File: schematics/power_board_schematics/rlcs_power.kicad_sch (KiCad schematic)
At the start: 39 parts, among them J1 Conn_01x05_Male, J2 Conn_01x05_Male, J4 Battery Conn, J5 Battery Conn, J6 CONN_01X02, J7 CONN_01X02, J8 CONN_01X02, Q1 Q_NPN_BEC, Q2 Q_NPN_BEC, T1 12 to 3v3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

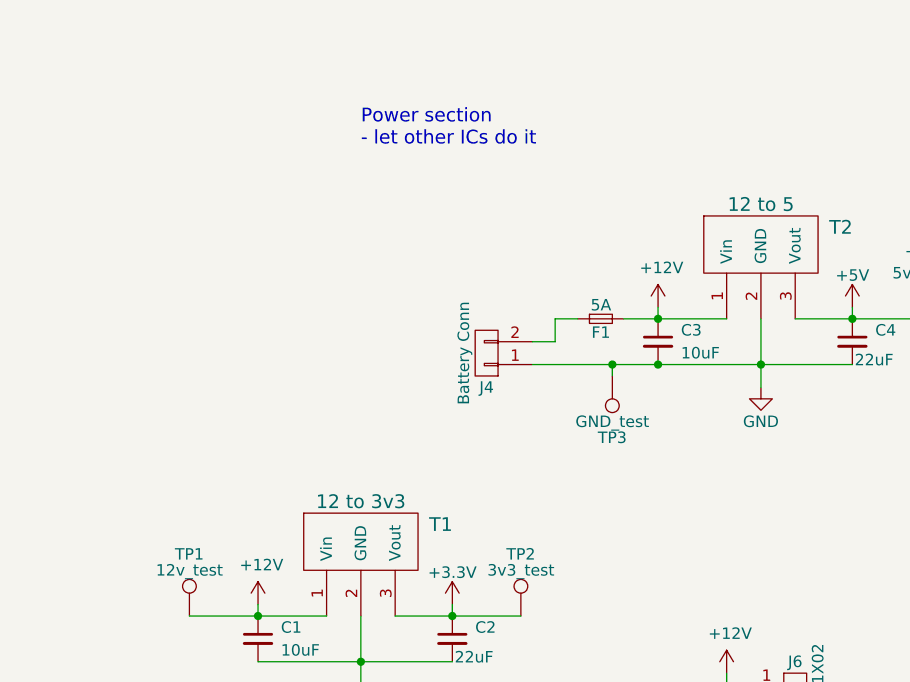
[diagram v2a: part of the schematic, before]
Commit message: Add Client Connection and Arm status indicator LED to Towerside Power Board schematic
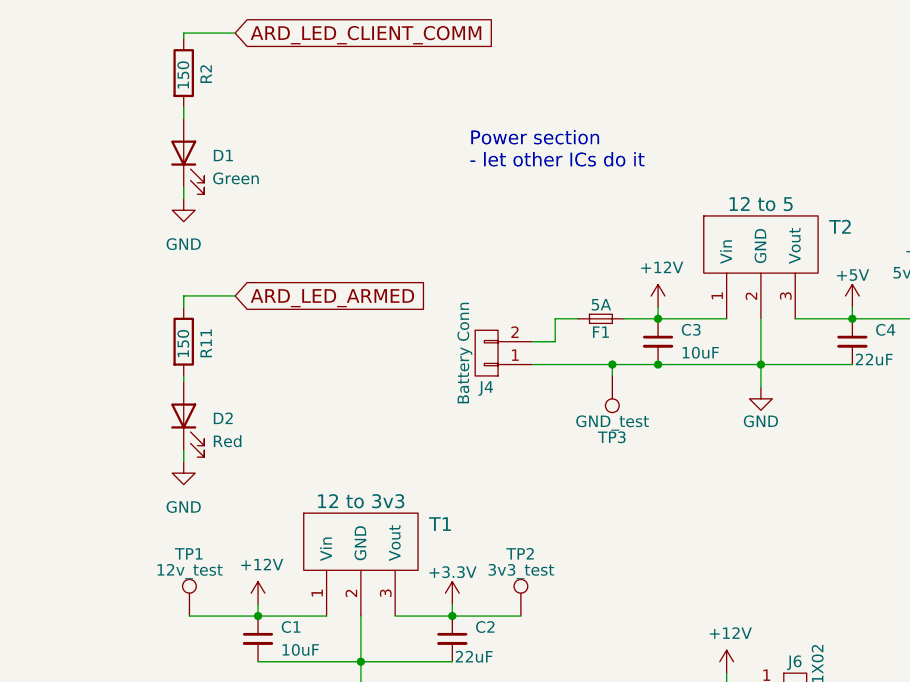
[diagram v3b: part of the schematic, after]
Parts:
- added D1: Green, LED_SMD:LED_1206_3216Metric_Pad1.42x1.75mm_HandSolder, symbol Device:LED
- added D2: Red, LED_SMD:LED_1206_3216Metric_Pad1.42x1.75mm_HandSolder, symbol Device:LED
- added R11, R2: 150, Resistor_SMD:R_0805_2012Metric_Pad1.20x1.40mm_HandSolder, symbol Device:R
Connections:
- net GND: now also D1.1 (K), D2.1 (K)
- new net: D1.2 (A), R2.2
- new net: D2.2 (A), R11.2
- new net ARD_LED_ARMED: R11.1
- new net ARD_LED_CLIENT_COMM: R2.1
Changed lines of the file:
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@@
+    (stroke (width 0) (type default) (color 0 0 0 0))
+  )
+  (wire (pts (xy 191.135 61.595) (xy 191.135 62.865))
     (stroke (width 0) (type default) (color 0 0 0 0))
   )
@@
     (stroke (width 0) (type default) (color 0 0 0 0))
   )
+  (wire (pts (xy 191.135 23.495) (xy 191.135 24.765))
+    (stroke (width 0) (type default) (color 0 0 0 0))
+  )
   (wire (pts (xy 46.99 129.54) (xy 46.99 123.19))
     (stroke (width 0) (type default) (color 0 0 0 0))
@@
     (stroke (width 0) (type default) (color 0 0 0 0))
   )
+  (wire (pts (xy 191.135 15.24) (xy 191.135 15.875))
+    (stroke (width 0) (type default) (color 0 0 0 0))
+  )
   (wire (pts (xy 251.46 149.86) (xy 248.92 149.86))
     (stroke (width 0) (type default) (color 0 0 0 0))
@@
     (stroke (width 0) (type default) (color 0 0 0 0))
   )
+  (wire (pts (xy 196.85 15.24) (xy 191.135 15.24))
+    (stroke (width 0) (type default) (color 0 0 0 0))
+  )
   (wire (pts (xy 243.84 52.07) (xy 255.27 52.07))
     (stroke (width 0) (type default) (color 0 0 0 0))
@@
     (stroke (width 0) (type default) (color 0 0 0 0))
   )
+  (wire (pts (xy 191.135 44.45) (xy 191.135 45.72))
+    (stroke (width 0) (type default) (color 0 0 0 0))
+  )
+  (wire (pts (xy 191.135 32.385) (xy 191.135 33.655))
+    (stroke (width 0) (type default) (color 0 0 0 0))
+  )
   (wire (pts (xy 139.7 158.75) (xy 139.7 181.61))
     (stroke (width 0) (type default) (color 0 0 0 0))
@@
     (stroke (width 0) (type default) (color 0 0 0 0))
   )
+  (wire (pts (xy 196.85 44.45) (xy 191.135 44.45))
+    (stroke (width 0) (type default) (color 0 0 0 0))
+  )
   (wire (pts (xy 127 166.37) (xy 113.03 166.37))
     (stroke (width 0) (type default) (color 0 0 0 0))
@@
   )
   (wire (pts (xy 251.46 127) (xy 251.46 128.27))
+    (stroke (width 0) (type default) (color 0 0 0 0))
+  )
+  (wire (pts (xy 191.135 53.34) (xy 191.135 53.975))
     (stroke (width 0) (type default) (color 0 0 0 0))
   )
@@
     (effects (font (size 1.524 1.524)) (justify left bottom))
   )
-  (text "Power section\n- let other ICs do it\n" (at 210.82 27.94 0)
+  (text "Power section\n- let other ICs do it\n" (at 222.885 30.48 0)
     (effects (font (size 1.524 1.524)) (justify left bottom))
   )
@@
     )
   )
+  (global_label "ARD_LED_CLIENT_COMM" (shape input) (at 196.85 15.24 0) (fields_autoplaced)
+    (effects (font (size 1.524 1.524)) (justify left))
+    (property "Intersheet References" "${INTERSHEET_REFS}" (id 0) (at 225.8372 15.1448 0)
+      (effects (font (size 1.524 1.524)) (justify left) hide)
+    )
+  )
   (global_label "Sevenseg_C" (shape input) (at 38.1 133.35 180) (fields_autoplaced)
     (effects (font (size 1.524 1.524)) (justify right))
@@
     (effects (font (size 1.524 1.524)) (justify left))
     (property "Intersheet References" "${INTERSHEET_REFS}" (id 0) (at 228.5949 118.0148 0)
+      (effects (font (size 1.524 1.524)) (justify left) hide)
+    )
+  )
+  (global_label "ARD_LED_ARMED" (shape input) (at 196.85 44.45 0) (fields_autoplaced)
+    (effects (font (size 1.524 1.524)) (justify left))
+    (property "Intersheet References" "${INTERSHEET_REFS}" (id 0) (at 217.9269 44.3548 0)
       (effects (font (size 1.524 1.524)) (justify left) hide)
     )
@@
     (pin "1")
   )
+  (symbol (lib_id "Device:LED") (at 191.135 28.575 90) (unit 1)
+    (in_bom yes) (on_board yes) (fields_autoplaced)
+    (property "Reference" "D1" (id 0) (at 194.31 28.8924 90)
+      (effects (font (size 1.27 1.27)) (justify right))
+    )
+    (property "Value" "Green" (id 1) (at 194.31 31.4324 90)
+      (effects (font (size 1.27 1.27)) (justify right))
+    )
+    (property "Footprint" "LED_SMD:LED_1206_3216Metric_Pad1.42x1.75mm_HandSolder" (id 2) (at 191.135 28.575 0)
+      (effects (font (size 1.27 1.27)) hide)
+    )
+    (property "Datasheet" "~" (id 3) (at 191.135 28.575 0)
+      (effects (font (size 1.27 1.27)) hide)
+    )
+    (pin "1")
+    (pin "2")
+  )
   (symbol (lib_id "Device:R") (at 53.34 162.56 90) (unit 1)
     (in_bom yes) (on_board yes)
@@
     (pin "1")
   )
+  (symbol (lib_id "Device:LED") (at 191.135 57.785 90) (unit 1)
+    (in_bom yes) (on_board yes) (fields_autoplaced)
+    (property "Reference" "D2" (id 0) (at 194.31 58.1024 90)
+      (effects (font (size 1.27 1.27)) (justify right))
+    )
+    (property "Value" "Red" (id 1) (at 194.31 60.6424 90)
+      (effects (font (size 1.27 1.27)) (justify right))
+    )
+    (property "Footprint" "LED_SMD:LED_1206_3216Metric_Pad1.42x1.75mm_HandSolder" (id 2) (at 191.135 57.785 0)
+      (effects (font (size 1.27 1.27)) hide)
+    )
+    (property "Datasheet" "~" (id 3) (at 191.135 57.785 0)
+      (effects (font (size 1.27 1.27)) hide)
+    )
+    (pin "1")
+    (pin "2")
+  )
+  (symbol (lib_id "Device:R") (at 191.135 49.53 0) (unit 1)
+    (in_bom yes) (on_board yes)
+    (property "Reference" "R11" (id 0) (at 193.675 51.435 90)
+      (effects (font (size 1.27 1.27)) (justify left))
+    )
+    (property "Value" "150" (id 1) (at 191.135 51.435 90)
+      (effects (font (size 1.27 1.27)) (justify left))
+    )
+    (property "Footprint" "Resistor_SMD:R_0805_2012Metric_Pad1.20x1.40mm_HandSolder" (id 2) (at 189.357 49.53 90)
+      (effects (font (size 1.27 1.27)) hide)
+    )
+    (property "Datasheet" "~" (id 3) (at 191.135 49.53 0)
+      (effects (font (size 1.27 1.27)) hide)
+    )
+    (pin "1")
+    (pin "2")
+  )
   (symbol (lib_id "Device:R") (at 138.43 123.19 0) (unit 1)
     (in_bom yes) (on_board yes)
@@
     (pin "1")
     (pin "2")
+  )
+  (symbol (lib_id "power:GND") (at 191.135 33.655 0) (unit 1)
+    (in_bom yes) (on_board yes) (fields_autoplaced)
+    (property "Reference" "#PWR0101" (id 0) (at 191.135 40.005 0)
+      (effects (font (size 1.27 1.27)) hide)
+    )
+    (property "Value" "GND" (id 1) (at 191.135 38.735 0))
+    (property "Footprint" "" (id 2) (at 191.135 33.655 0)
+      (effects (font (size 1.27 1.27)) hide)
+    )
+    (property "Datasheet" "" (id 3) (at 191.135 33.655 0)
+      (effects (font (size 1.27 1.27)) hide)
+    )
+    (pin "1")
   )
   (symbol (lib_id "Device:R") (at 72.39 102.87 90) (unit 1)
@@
     )
     (property "Datasheet" "" (id 3) (at 243.84 151.13 0)
+      (effects (font (size 1.27 1.27)) hide)
+    )
+    (pin "1")
+    (pin "2")
+  )
+  (symbol (lib_id "power:GND") (at 191.135 62.865 0) (unit 1)
+    (in_bom yes) (on_board yes) (fields_autoplaced)
+    (property "Reference" "#PWR0102" (id 0) (at 191.135 69.215 0)
+      (effects (font (size 1.27 1.27)) hide)
+    )
+    (property "Value" "GND" (id 1) (at 191.135 67.945 0))
+    (property "Footprint" "" (id 2) (at 191.135 62.865 0)
+      (effects (font (size 1.27 1.27)) hide)
+    )
+    (property "Datasheet" "" (id 3) (at 191.135 62.865 0)
+      (effects (font (size 1.27 1.27)) hide)
+    )
+    (pin "1")
+  )
+  (symbol (lib_id "Device:R") (at 191.135 19.685 0) (unit 1)
+    (in_bom yes) (on_board yes)
+    (property "Reference" "R2" (id 0) (at 193.675 20.955 90)
+      (effects (font (size 1.27 1.27)) (justify left))
+    )
+    (property "Value" "150" (id 1) (at 191.135 21.59 90)
+      (effects (font (size 1.27 1.27)) (justify left))
+    )
+    (property "Footprint" "Resistor_SMD:R_0805_2012Metric_Pad1.20x1.40mm_HandSolder" (id 2) (at 189.357 19.685 90)
+      (effects (font (size 1.27 1.27)) hide)
+    )
+    (property "Datasheet" "~" (id 3) (at 191.135 19.685 0)
       (effects (font (size 1.27 1.27)) hide)
     )
@@
       (reference "#PWR039") (unit 1) (value "GND") (footprint "")
     )
+    (path "/7fb8ef43-d65f-44dd-ae9c-507b7c0f88c3"
+      (reference "#PWR0101") (unit 1) (value "GND") (footprint "")
+    )
+    (path "/c2bf3841-8388-4aad-ad61-1e36374412b8"
+      (reference "#PWR0102") (unit 1) (value "GND") (footprint "")
+    )
     (path "/00000000-0000-0000-0000-000059c5bada"
       (reference "AFF1") (unit 1) (value "LTD-4608JR") (footprint "rlcs_power:LTD-4608JR")
@@
       (reference "C4") (unit 1) (value "22uF") (footprint "Capacitor_SMD:C_0805_2012Metric_Pad1.15x1.40mm_HandSolder")
     )
+    (path "/38aefd43-baab-49f7-894b-b02c0f5ad5f8"
+      (reference "D1") (unit 1) (value "Green") (footprint "LED_SMD:LED_1206_3216Metric_Pad1.42x1.75mm_HandSolder")
+    )
+    (path "/7290a19e-b927-4c95-8e9d-ef79eaffaa7f"
+      (reference "D2") (unit 1) (value "Red") (footprint "LED_SMD:LED_1206_3216Metric_Pad1.42x1.75mm_HandSolder")
+    )
     (path "/00000000-0000-0000-0000-000059b5bfb2"
       (reference "F1") (unit 1) (value "5A") (footprint "Fuse_Holders_and_Fuses:Fuseholder5x20_horiz_open_inline_Type-I")
@@
       (reference "R1") (unit 1) (value "5k") (footprint "Resistor_SMD:R_0805_2012Metric_Pad1.20x1.40mm_HandSolder")
     )
+    (path "/dfdb4d2f-59f9-4078-a9cc-40d2b8cce980"
+      (reference "R2") (unit 1) (value "150") (footprint "Resistor_SMD:R_0805_2012Metric_Pad1.20x1.40mm_HandSolder")
+    )
     (path "/00000000-0000-0000-0000-000059c44db4"
       (reference "R3") (unit 1) (value "150") (footprint "Resistor_SMD:R_0805_2012Metric_Pad1.20x1.40mm_HandSolder")
@@
       (reference "R10") (unit 1) (value "150") (footprint "Resistor_SMD:R_0805_2012Metric_Pad1.20x1.40mm_HandSolder")
     )
+    (path "/73b5e225-ae20-471d-bb2e-6e53d824d522"
+      (reference "R11") (unit 1) (value "150") (footprint "Resistor_SMD:R_0805_2012Metric_Pad1.20x1.40mm_HandSolder")
+    )
     (path "/87ca7689-6283-42ef-8729-0d414fc30675"

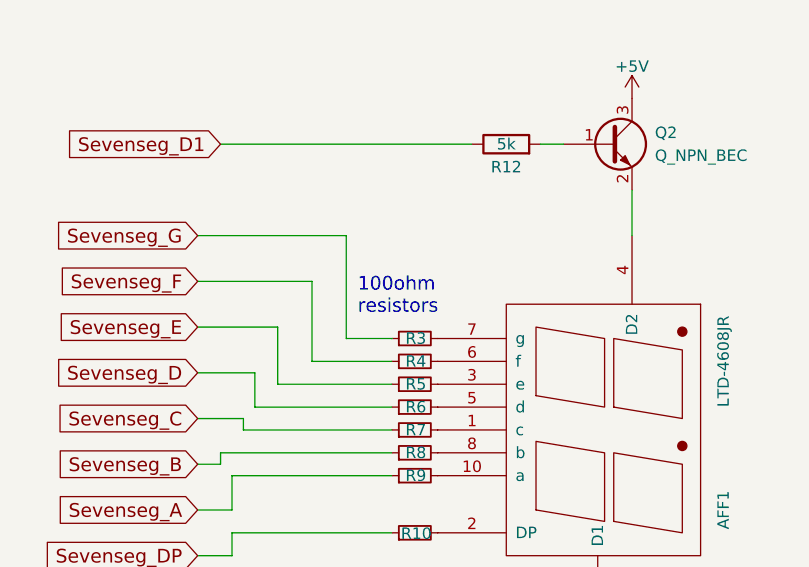
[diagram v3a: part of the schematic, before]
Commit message: Fix resistor label typo in Towerside Power Board schematic
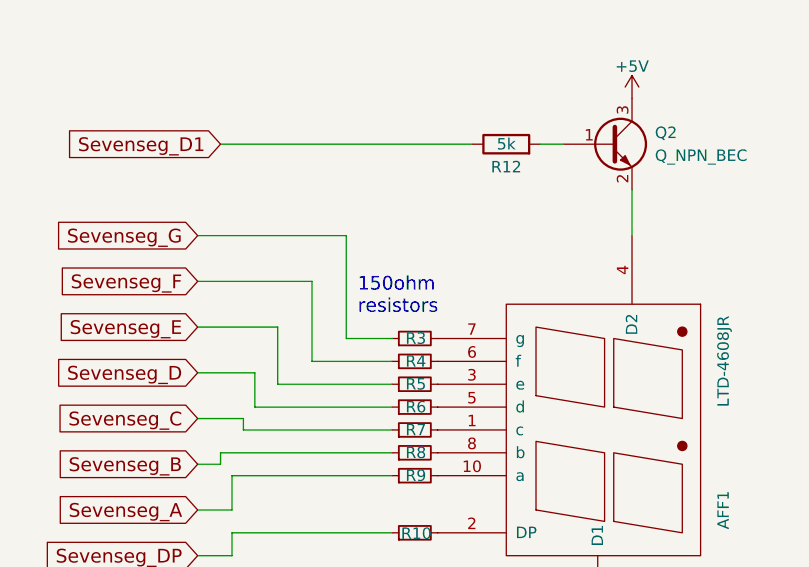
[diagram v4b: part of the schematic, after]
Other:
- note added: "150ohm resistors"
- note removed: "100ohm resistors"
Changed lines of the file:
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@@
     (effects (font (size 1.524 1.524)) (justify left bottom))
   )
-  (text "100ohm\nresistors\n" (at 55.88 121.92 0)
+  (text "150ohm\nresistors\n" (at 55.88 121.92 0)
     (effects (font (size 1.524 1.524)) (justify left bottom))
   )

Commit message: Add UART connector to Towerside Power Board schematic
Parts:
- added J3: Screw_Terminal_01x02, TerminalBlock_Phoenix:TerminalBlock_Phoenix_PT-1,5-2-5.0-H_1x02_P5.00mm_Horizontal, symbol Connector:Screw_Terminal_01x02
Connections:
- new net ARD_UART_RX: J3.1 (Pin_1)
- new net ARD_UART_TX: J3.2 (Pin_2)
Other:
- note added: "UART Connector"
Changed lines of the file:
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@@
+    (stroke (width 0) (type default) (color 0 0 0 0))
+  )
+  (wire (pts (xy 161.925 97.155) (xy 170.815 97.155))
     (stroke (width 0) (type default) (color 0 0 0 0))
   )
@@
   )
   (wire (pts (xy 50.8 127) (xy 50.8 118.11))
+    (stroke (width 0) (type default) (color 0 0 0 0))
+  )
+  (wire (pts (xy 161.925 94.615) (xy 170.815 94.615))
     (stroke (width 0) (type default) (color 0 0 0 0))
   )
@@
     (effects (font (size 1.524 1.524)) (justify left bottom))
   )
+  (text "UART Connector" (at 165.735 90.17 0)
+    (effects (font (size 1.524 1.524)) (justify left bottom))
+  )
   (text "150ohm\nresistors\n" (at 55.88 121.92 0)
     (effects (font (size 1.524 1.524)) (justify left bottom))
@@
   (label "ACTUATOR_BAT" (at 138.43 106.68 180)
     (effects (font (size 1.524 1.524)) (justify right bottom))
+  )
+  (global_label "ARD_UART_TX" (shape input) (at 170.815 97.155 0) (fields_autoplaced)
+    (effects (font (size 1.524 1.524)) (justify left))
+    (property "Intersheet References" "${INTERSHEET_REFS}" (id 0) (at 188.481 97.0598 0)
+      (effects (font (size 1.524 1.524)) (justify left) hide)
+    )
   )
   (global_label "Sevenseg_D" (shape input) (at 38.1 128.27 180) (fields_autoplaced)
@@
     (property "Intersheet References" "${INTERSHEET_REFS}" (id 0) (at -8.89 0 0)
       (effects (font (size 1.27 1.27)) hide)
+    )
+  )
+  (global_label "ARD_UART_RX" (shape input) (at 170.815 94.615 0) (fields_autoplaced)
+    (effects (font (size 1.524 1.524)) (justify left))
+    (property "Intersheet References" "${INTERSHEET_REFS}" (id 0) (at 188.8439 94.5198 0)
+      (effects (font (size 1.524 1.524)) (justify left) hide)
     )
   )
@@
     (pin "1")
   )
+  (symbol (lib_id "Connector:Screw_Terminal_01x02") (at 156.845 94.615 0) (mirror y) (unit 1)
+    (in_bom yes) (on_board yes)
+    (property "Reference" "J3" (id 0) (at 156.845 90.17 0))
+    (property "Value" "Screw_Terminal_01x02" (id 1) (at 156.845 92.075 0))
+    (property "Footprint" "TerminalBlock_Phoenix:TerminalBlock_Phoenix_PT-1,5-2-5.0-H_1x02_P5.00mm_Horizontal" (id 2) (at 156.845 94.615 0)
+      (effects (font (size 1.27 1.27)) hide)
+    )
+    (property "Datasheet" "~" (id 3) (at 156.845 94.615 0)
+      (effects (font (size 1.27 1.27)) hide)
+    )
+    (pin "1")
+    (pin "2")
+  )
   (symbol (lib_id "Device:R") (at 191.135 19.685 0) (unit 1)
     (in_bom yes) (on_board yes)
@@
       (reference "J2") (unit 1) (value "Conn_01x05_Male") (footprint "Connector_JST:JST_EH_B5B-EH-A_1x05_P2.50mm_Vertical")
     )
+    (path "/dd654b78-9c0d-41b7-ad5c-a9ae8bc2ff19"
+      (reference "J3") (unit 1) (value "Screw_Terminal_01x02") (footprint "TerminalBlock_Phoenix:TerminalBlock_Phoenix_PT-1,5-2-5.0-H_1x02_P5.00mm_Horizontal")
+    )
     (path "/00000000-0000-0000-0000-000059b5bf44"
